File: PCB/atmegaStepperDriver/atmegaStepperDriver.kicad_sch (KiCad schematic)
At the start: 79 parts, among them J1 General power, J2 Motor Output, J3 Motor power, J4 Conn_01x02_Pin, J5 Reset Header, J6 I2C Communication pins, J8 Conn_01x06_Socket, J9 Stepper communication pins, Q1 TIP42C, Q10 BC547, Q11 BC557, Q12 TIP41C, Q13 TIP42C, Q14 BC547, Q15 BC557, Q16 TIP41C, Q17 BC547, Q2 TIP41C, Q3 TIP42C, Q4 TIP42C, Q5 BC547, Q6 BC547, Q7 BC557, Q8 TIP41C, Q9 BC557, U1 ATmega328P-P, U2 LM7805_TO220, Y1 Crystal

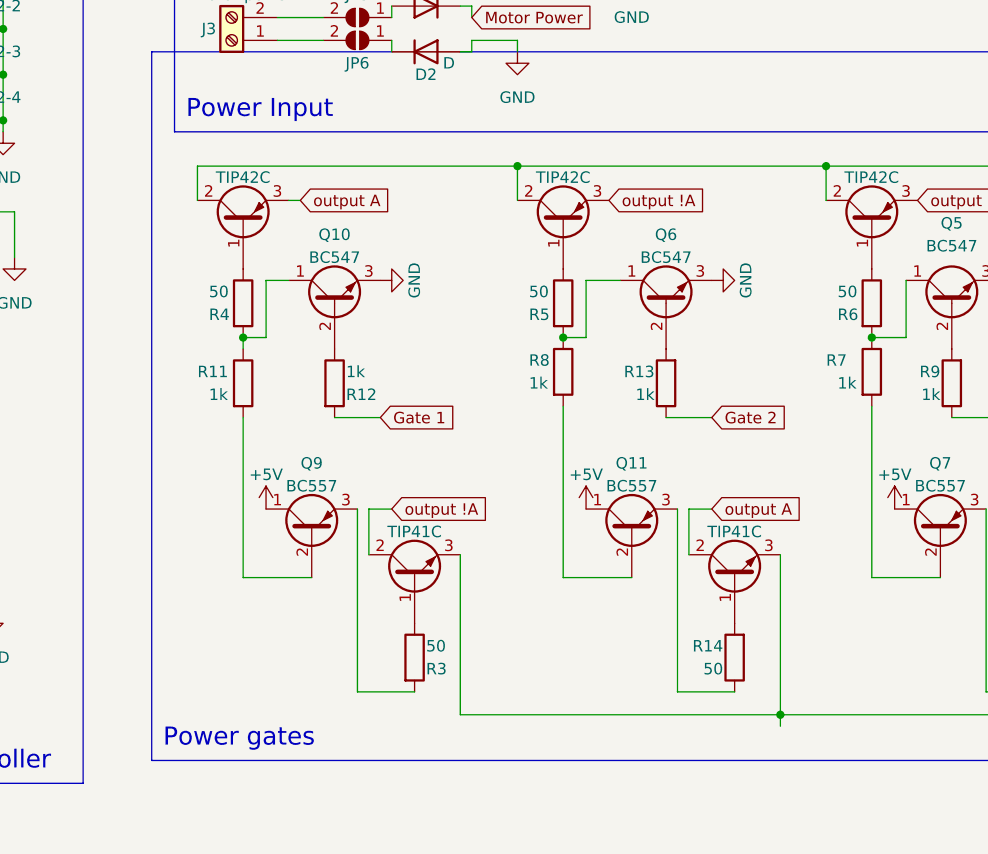
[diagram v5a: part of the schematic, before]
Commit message: posible fix, need more research + for the streak
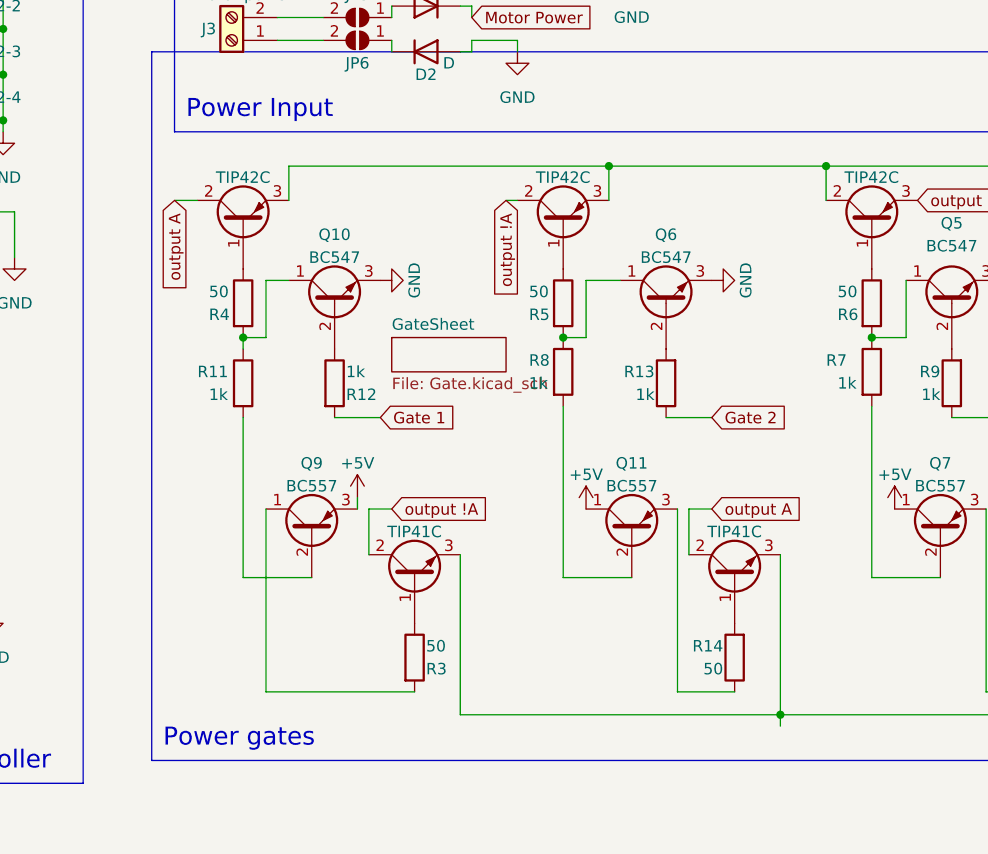
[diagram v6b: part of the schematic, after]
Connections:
- net +5V: now also Q9.3 (E); no longer Q9.1 (C)
- net Motor Power: now also Q1.3 (E), Q3.3 (E); no longer Q1.2 (C), Q3.2 (C)
- net output !A: now also Q3.2 (C); no longer Q3.3 (E)
- net output A: now also Q1.2 (C); no longer Q1.3 (E)
- net at R3.2: now also Q9.1 (C); no longer Q9.3 (E)
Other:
- added sheet GateSheet (Gate.kicad_sch)
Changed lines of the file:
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@@
   (junction (at 71.12 38.1) (diameter 0) (color 0 0 0 0)
   )
+  (junction (at 168.91 58.42) (diameter 0) (color 0 0 0 0)
+  )
   (junction (at 240.03 39.37) (diameter 0) (color 0 0 0 0)
   )
@@
   (junction (at 95.25 180.34) (diameter 0) (color 0 0 0 0)
   )
-  (junction (at 158.75 58.42) (diameter 0) (color 0 0 0 0)
-  )
   (junction (at 81.28 143.51) (diameter 0) (color 0 0 0 0)
   )
@@
   (junction (at 72.39 85.09) (diameter 0) (color 0 0 0 0)
   )
+  (wire (pts (xy 133.35 58.42) (xy 133.35 62.23))
+    (stroke (width 0) (type default))
+  )
   (wire (pts (xy 176.53 116.84) (xy 182.88 116.84))
     (stroke (width 0) (type default))
@@
     (stroke (width 0) (type default))
   )
-  (wire (pts (xy 123.19 58.42) (xy 158.75 58.42))
-    (stroke (width 0) (type default))
-  )
   (wire (pts (xy 195.58 20.32) (xy 194.31 20.32))
     (stroke (width 0) (type default))
@@
     (stroke (width 0) (type default))
   )
+  (wire (pts (xy 157.48 62.23) (xy 158.75 62.23))
+    (stroke (width 0) (type default))
+  )
   (wire (pts (xy 100.33 180.34) (xy 100.33 167.64))
     (stroke (width 0) (type default))
@@
     (stroke (width 0) (type default))
   )
+  (wire (pts (xy 168.91 58.42) (xy 193.04 58.42))
+    (stroke (width 0) (type default))
+  )
   (wire (pts (xy 152.4 45.72) (xy 153.67 45.72))
     (stroke (width 0) (type default))
@@
     (stroke (width 0) (type default))
   )
-  (wire (pts (xy 123.19 58.42) (xy 123.19 62.23))
-    (stroke (width 0) (type default))
-  )
   (wire (pts (xy 132.08 44.45) (xy 137.16 44.45))
     (stroke (width 0) (type default))
@@
     (stroke (width 0) (type default))
   )
+  (wire (pts (xy 140.97 95.25) (xy 140.97 96.52))
+    (stroke (width 0) (type default))
+  )
   (wire (pts (xy 195.58 154.94) (xy 195.58 153.67))
     (stroke (width 0) (type default))
@@
     (stroke (width 0) (type default))
   )
+  (wire (pts (xy 168.91 62.23) (xy 168.91 58.42))
+    (stroke (width 0) (type default))
+  )
   (wire (pts (xy 54.61 62.23) (xy 64.77 62.23))
     (stroke (width 0) (type default))
@@
     (stroke (width 0) (type default))
   )
-  (wire (pts (xy 140.97 96.52) (xy 140.97 116.84))
-    (stroke (width 0) (type default))
-  )
   (wire (pts (xy 194.31 143.51) (xy 194.31 142.24))
     (stroke (width 0) (type default))
@@
     (stroke (width 0) (type default))
   )
-  (wire (pts (xy 57.15 107.95) (xy 57.15 110.49))
+  (wire (pts (xy 133.35 58.42) (xy 168.91 58.42))
     (stroke (width 0) (type default))
   )
-  (wire (pts (xy 54.61 92.71) (xy 60.96 92.71))
+  (wire (pts (xy 57.15 107.95) (xy 57.15 110.49))
     (stroke (width 0) (type default))
   )
-  (wire (pts (xy 134.62 62.23) (xy 133.35 62.23))
+  (wire (pts (xy 54.61 92.71) (xy 60.96 92.71))
     (stroke (width 0) (type default))
   )
@@
     (stroke (width 0) (type default))
   )
-  (wire (pts (xy 147.32 116.84) (xy 140.97 116.84))
+  (wire (pts (xy 130.81 116.84) (xy 147.32 116.84))
     (stroke (width 0) (type default))
   )
@@
     (stroke (width 0) (type default))
   )
+  (wire (pts (xy 130.81 116.84) (xy 130.81 96.52))
+    (stroke (width 0) (type default))
+  )
   (wire (pts (xy 38.1 154.94) (xy 38.1 163.83))
     (stroke (width 0) (type default))
@@
     (stroke (width 0) (type default))
   )
+  (wire (pts (xy 120.65 62.23) (xy 123.19 62.23))
+    (stroke (width 0) (type default))
+  )
   (wire (pts (xy 83.82 45.72) (xy 69.85 45.72))
     (stroke (width 0) (type default))
@@
     (stroke (width 0) (type default))
   )
-  (wire (pts (xy 158.75 58.42) (xy 193.04 58.42))
-    (stroke (width 0) (type default))
-  )
   (wire (pts (xy 68.58 167.64) (xy 74.93 167.64))
     (stroke (width 0) (type default))
@@
     (stroke (width 0) (type default))
   )
-  (wire (pts (xy 158.75 58.42) (xy 158.75 62.23))
-    (stroke (width 0) (type default))
-  )
   (wire (pts (xy 93.98 63.5) (xy 93.98 67.31))
     (stroke (width 0) (type default))
@@
     )
   )
-  (global_label "output A" (shape input) (at 134.62 62.23 0) (fields_autoplaced)
-    (effects (font (size 1.27 1.27)) (justify left))
-    (property "Intersheetrefs" "${INTERSHEET_REFS}" (at 145.7088 62.23 0)
-      (effects (font (size 1.27 1.27)) (justify left) hide)
+  (global_label "output A" (shape input) (at 120.65 62.23 270) (fields_autoplaced)
+    (effects (font (size 1.27 1.27)) (justify right))
+    (property "Intersheetrefs" "${INTERSHEET_REFS}" (at 120.65 73.3188 90)
+      (effects (font (size 1.27 1.27)) (justify right) hide)
     )
   )
-  (global_label "output !A" (shape input) (at 168.91 62.23 0) (fields_autoplaced)
-    (effects (font (size 1.27 1.27)) (justify left))
-    (property "Intersheetrefs" "${INTERSHEET_REFS}" (at 180.6036 62.23 0)
-      (effects (font (size 1.27 1.27)) (justify left) hide)
+  (global_label "output !A" (shape input) (at 157.48 62.23 270) (fields_autoplaced)
+    (effects (font (size 1.27 1.27)) (justify right))
+    (property "Intersheetrefs" "${INTERSHEET_REFS}" (at 157.48 73.9236 90)
+      (effects (font (size 1.27 1.27)) (justify right) hide)
     )
   )
@@
     )
   )
-  (symbol (lib_id "power:+5V") (at 130.81 96.52 0) (unit 1)
+  (symbol (lib_id "power:+5V") (at 140.97 95.25 0) (unit 1)
     (in_bom yes) (on_board yes) (dnp no)
-    (property "Reference" "#PWR012" (at 130.81 100.33 0)
+    (property "Reference" "#PWR012" (at 140.97 99.06 0)
       (effects (font (size 1.27 1.27)) hide)
     )
-    (property "Value" "+5V" (at 130.81 92.71 0)
+    (property "Value" "+5V" (at 140.97 91.44 0)
       (effects (font (size 1.27 1.27)))
     )
-    (property "Footprint" "" (at 130.81 96.52 0)
+    (property "Footprint" "" (at 140.97 95.25 0)
       (effects (font (size 1.27 1.27)) hide)
     )
-    (property "Datasheet" "" (at 130.81 96.52 0)
+    (property "Datasheet" "" (at 140.97 95.25 0)
       (effects (font (size 1.27 1.27)) hide)
     )
@@
       )
     )
+  )
+  (sheet (at 144.78 77.47) (size 12.7 3.81) (fields_autoplaced)
+    (stroke (width 0.1524) (type solid))
+    (fill (color 0 0 0 0.0000))
+    (property "Sheetname" "GateSheet" (at 144.78 76.7584 0)
+      (effects (font (size 1.27 1.27)) (justify left bottom))
+    )
+    (property "Sheetfile" "Gate.kicad_sch" (at 144.78 81.8646 0)
+      (effects (font (size 1.27 1.27)) (justify left top))
+    )
+    (instances
+      (project "atmegaStepperDriver"
+        (path "/c84e7e69-c1fd-4499-93bc-6ad0c4ebade1" (page "2"))
+      )
+    )

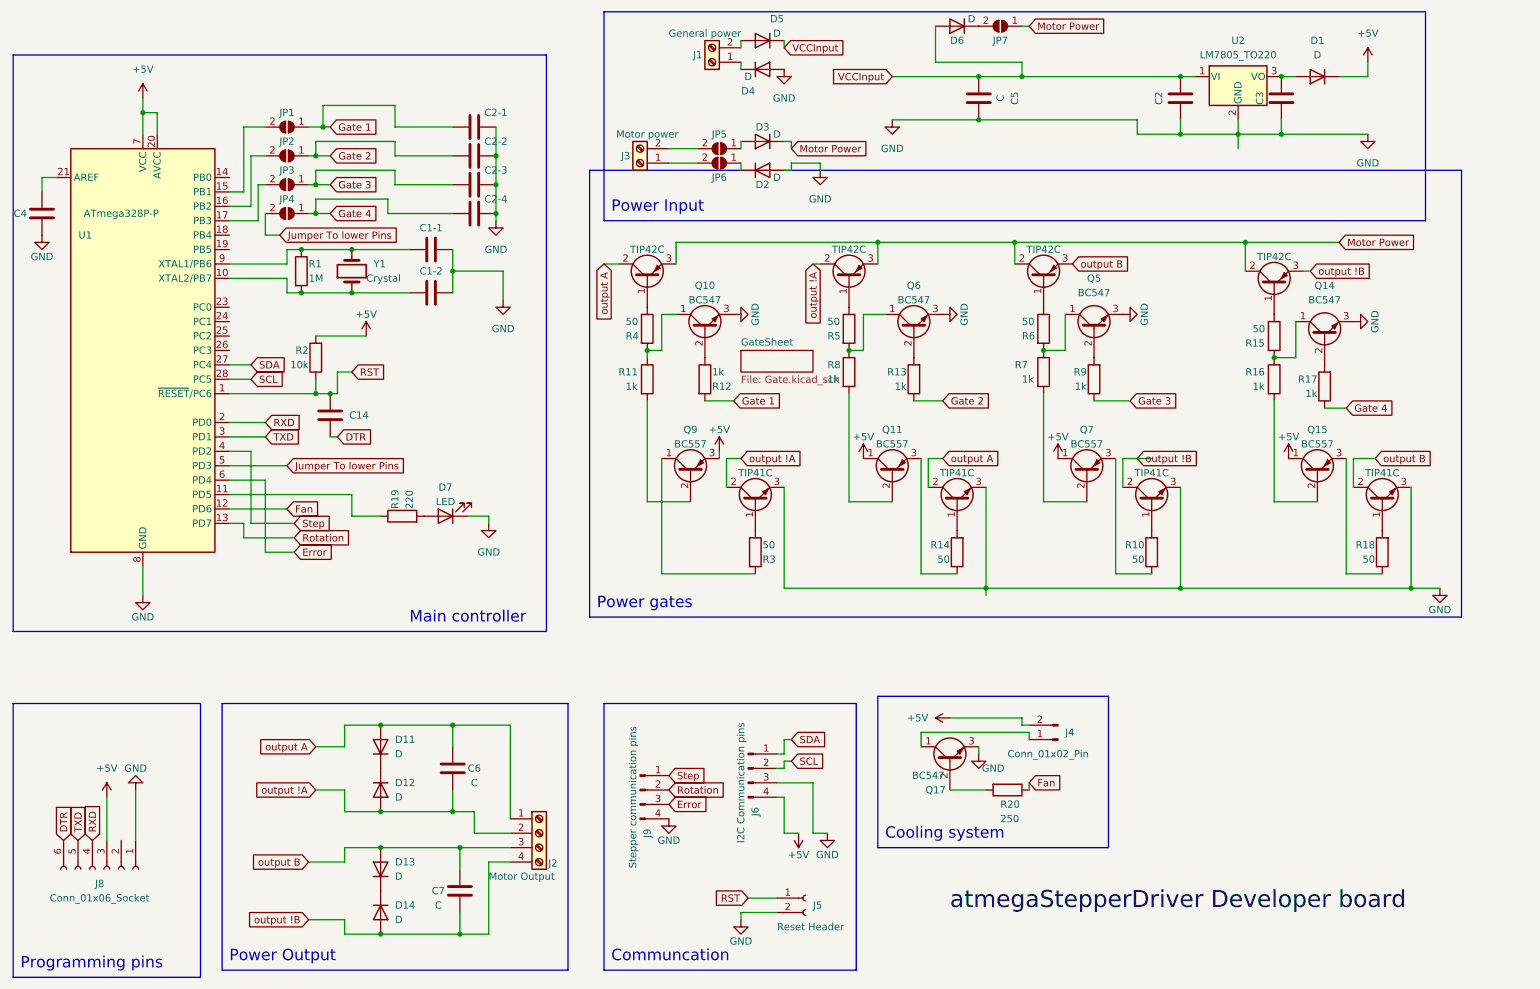
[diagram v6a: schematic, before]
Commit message: Fix gate; added termistor; gate sheet added; v0.8.4
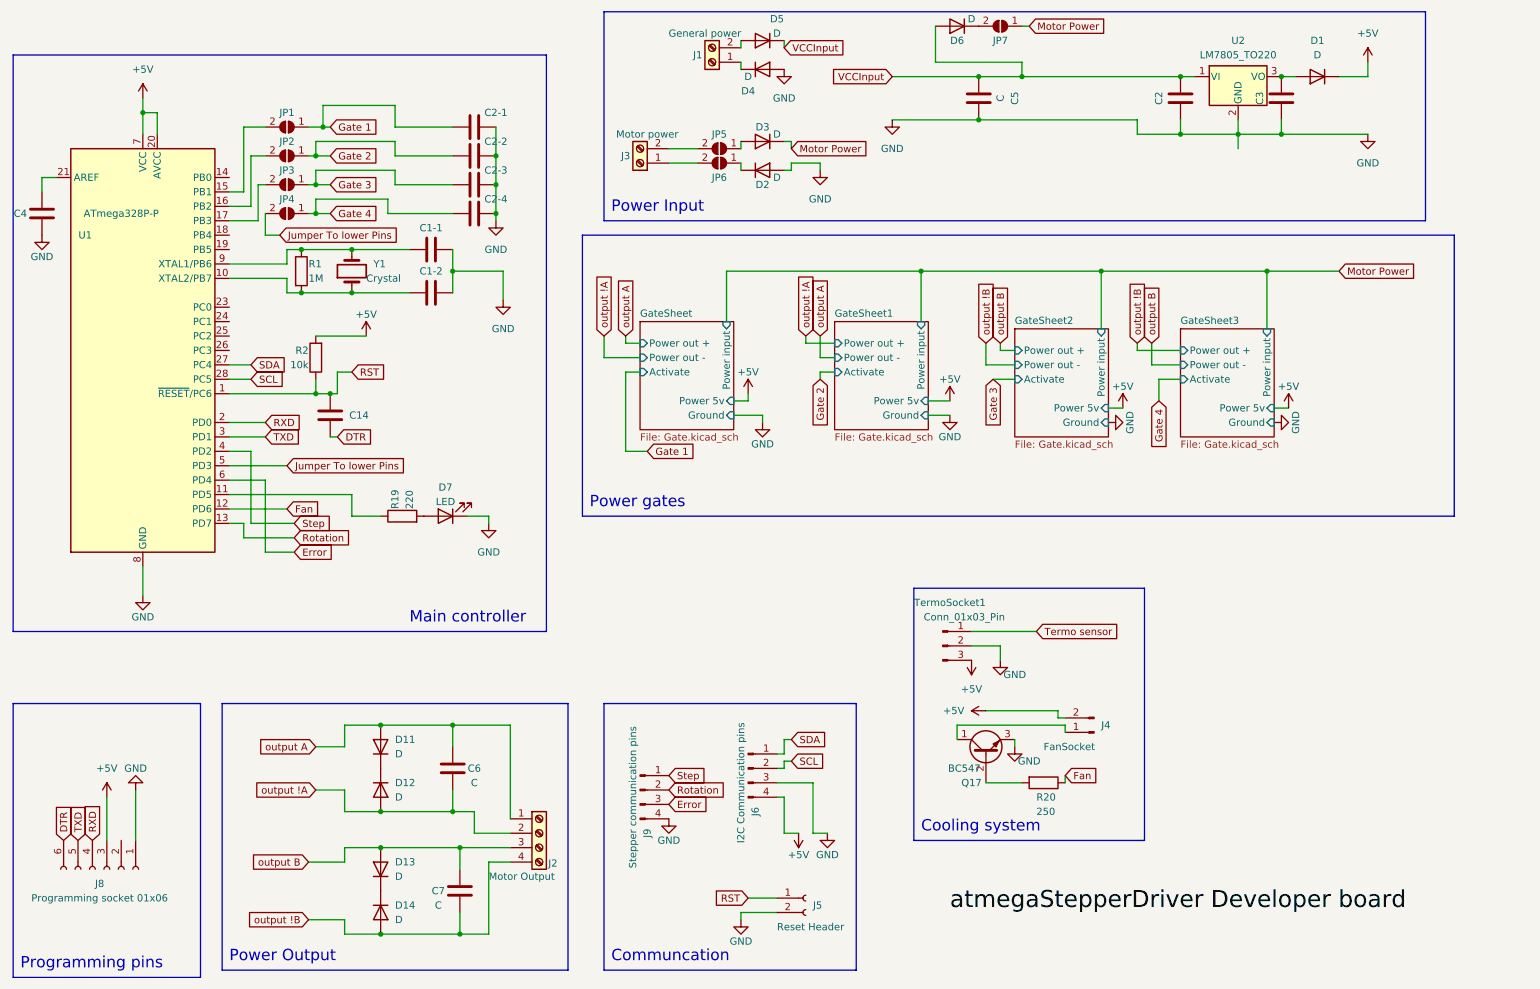
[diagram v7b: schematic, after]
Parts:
- removed Q1, Q13, Q3, Q4: TIP42C, Package_TO_SOT_THT:TO-220-3_Vertical, symbol Transistor_BJT:TIP42C
- removed Q10, Q14, Q5, Q6: BC547, Package_TO_SOT_THT:TO-92_Inline_Wide, symbol Transistor_BJT:BC547
- removed Q11, Q15, Q7, Q9: BC557, Package_TO_SOT_THT:TO-92_Inline_Wide, symbol Transistor_BJT:BC557
- removed Q12, Q16, Q2, Q8: TIP41C, Package_TO_SOT_THT:TO-220-3_Vertical, symbol Transistor_BJT:TIP41C
- removed R10, R14, R15, R18, R3, R4, R5, R6: 50, Resistor_THT:R_Axial_DIN0207_L6.3mm_D2.5mm_P10.16mm_Horizontal, symbol Device:R
- removed R11, R12, R13, R16, R17, R7, R8, R9: 1k, Resistor_THT:R_Axial_DIN0207_L6.3mm_D2.5mm_P10.16mm_Horizontal, symbol Device:R
- added TermoSocket1: Conn_01x03_Pin, Connector_PinHeader_2.54mm:PinHeader_1x03_P2.54mm_Vertical, symbol Connector:Conn_01x03_Pin
- J4: value Conn_01x02_Pin -> FanSocket
- J8: value Conn_01x06_Socket -> Programming socket 01x06
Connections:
- net +5V: now also TermoSocket1.3 (Pin_3)
- net GND: now also TermoSocket1.2 (Pin_2)
- new net Termo sensor: TermoSocket1.1 (Pin_1)
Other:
- added sheet GateSheet1 (Gate.kicad_sch)
- added sheet GateSheet2 (Gate.kicad_sch)
- added sheet GateSheet3 (Gate.kicad_sch)
- sheet GateSheet ports: added Activate, Ground, Power 5v, Power input, Power out +, Power out -; removed none
- moved on the sheet: J4, Q17, R20

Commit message: Reader for motor movement added; possible resistor on termistor
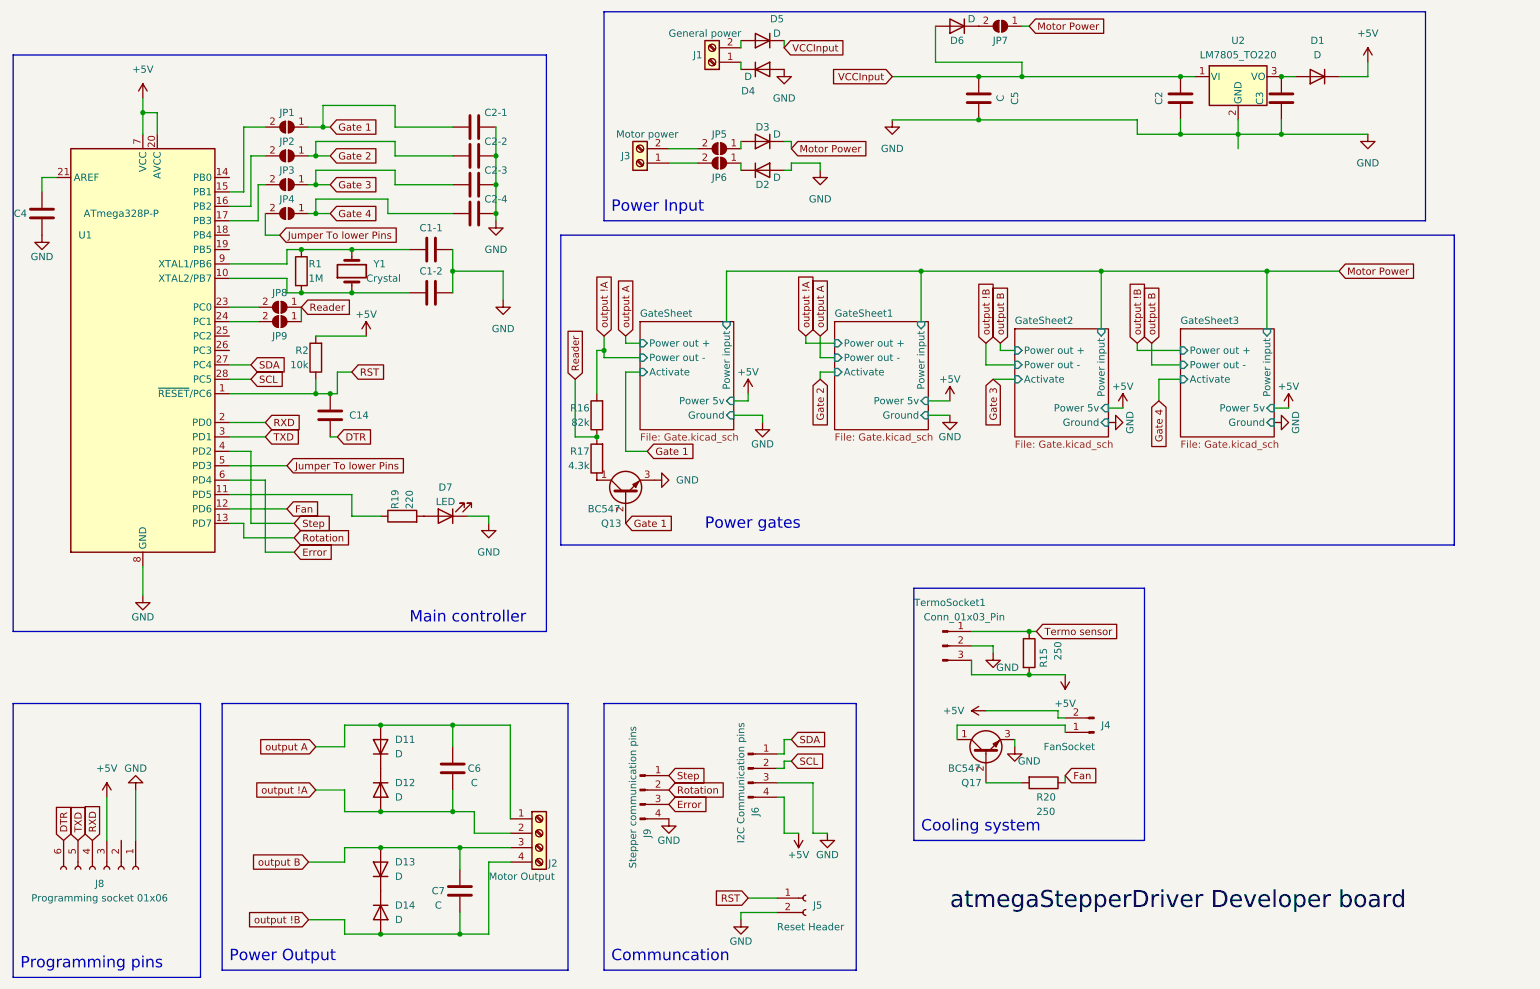
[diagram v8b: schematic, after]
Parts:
- added JP8, JP9: SolderJumper_2_Open, Jumper:SolderJumper-2_P1.3mm_Open_RoundedPad1.0x1.5mm, symbol Jumper:SolderJumper_2_Open
- added Q13: BC547, Package_TO_SOT_THT:TO-92_Inline, symbol Transistor_BJT:BC547
- added R15: 250, Resistor_THT:R_Axial_DIN0207_L6.3mm_D2.5mm_P10.16mm_Horizontal, symbol Device:R
- added R16: 82k, Resistor_THT:R_Axial_DIN0207_L6.3mm_D2.5mm_P10.16mm_Horizontal, symbol Device:R
- added R17: 4.3k, Resistor_THT:R_Axial_DIN0207_L6.3mm_D2.5mm_P10.16mm_Horizontal, symbol Device:R
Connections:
- net +5V: now also R15.2
- net GND: now also Q13.3 (E)
- net Gate 1: now also Q13.2 (B)
- net Termo sensor: now also R15.1
- net output !A: now also R16.2
- net at U1.23 (PC0): now also JP8.2 (B)
- net at U1.24 (PC1): now also JP9.2 (B)
- new net: Q13.1 (C), R17.1
- new net Reader: JP8.1 (A), JP9.1 (A), R16.1, R17.2
